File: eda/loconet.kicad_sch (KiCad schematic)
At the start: 78 parts, among them J1 RJ12, J10 DCC IN, J11 DCC1, J12 FROG3, J13 DCC4, J14 FROG4, J15 LN Debug, J16 LN Raw, J2 RJ12, J3 FROG1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

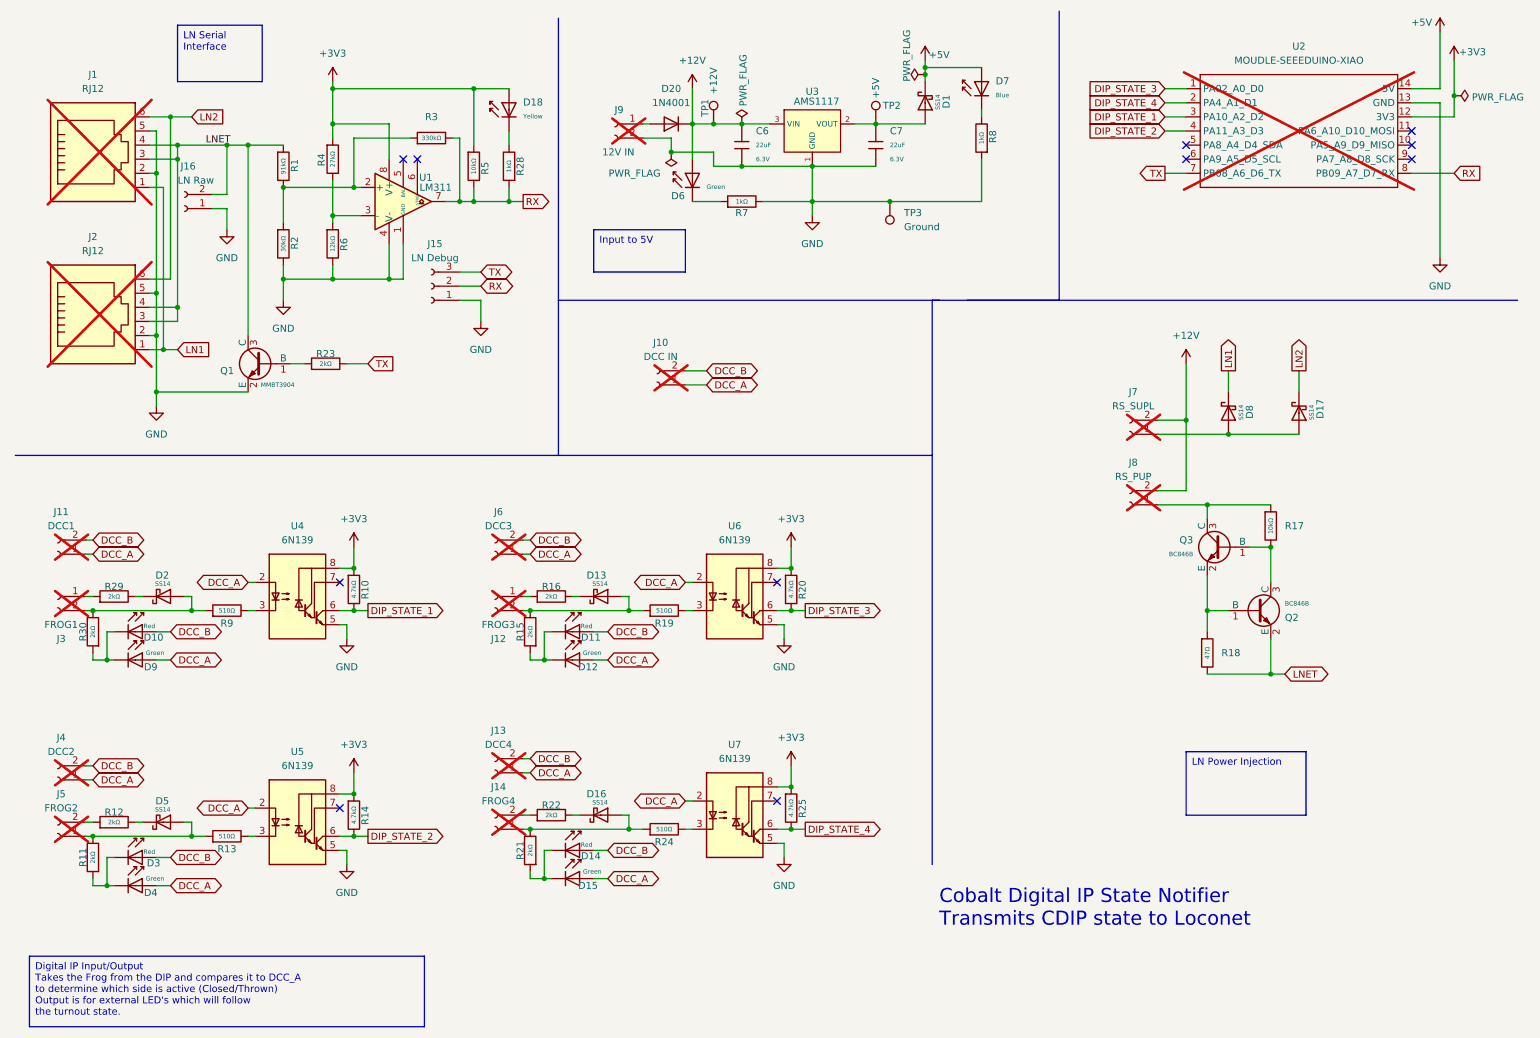
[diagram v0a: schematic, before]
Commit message: Fixups
* I removed the additional forwarding power part of the LN schematic. I don't think I was doing it right anyway. use a UP5 instead.
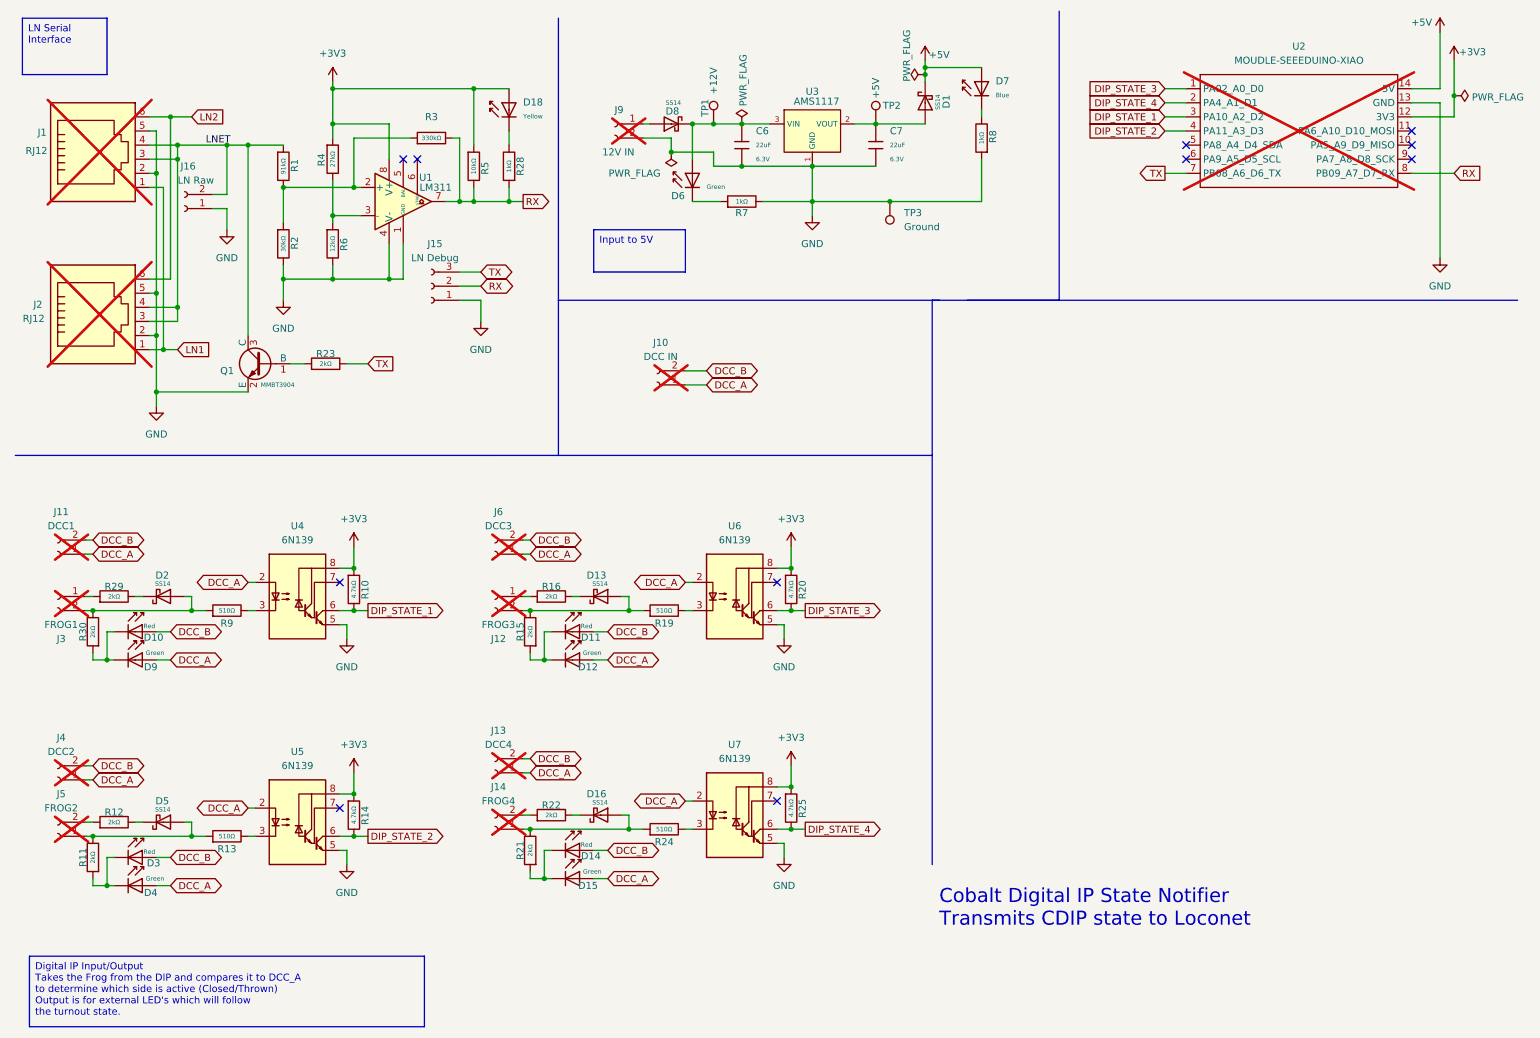
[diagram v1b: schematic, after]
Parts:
- removed D17: SS14, PCM_JLCPCB:D_SMA, symbol PCM_JLCPCB-Diodes:Schottky,SS14
- removed D20: 1N4001, Diode_THT:D_DO-41_SOD81_P10.16mm_Horizontal, symbol Diode:1N4001
- removed J7: RS_SUPL, Connector_PinHeader_2.54mm:PinHeader_1x02_P2.54mm_Vertical, symbol Connector:Conn_01x02_Socket
- removed J8: RS_PUP, Connector_PinHeader_2.54mm:PinHeader_1x02_P2.54mm_Vertical, symbol Connector:Conn_01x02_Socket
- removed Q2, Q3: BC846B, PCM_JLCPCB:Q_SOT-23, symbol PCM_JLCPCB-Transistors:NPN,BC846B
- removed R17: 10kΩ, PCM_JLCPCB:R_0603, symbol PCM_JLCPCB-Resistors:0603,10kΩ
- removed R18: 47Ω, PCM_JLCPCB:R_0603, symbol PCM_JLCPCB-Resistors:0603,47Ω
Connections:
- net LN1: no longer D8.1
- net at J9.1 (Pin_1): now also D8.2
- net +12V: no longer names the net of C6.1, D6.2, TP1.1, U3.3 (VIN)
- net +12V: now also D8.1

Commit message: Updating to the latest version of the board, still in KiCad 8.
* Bumped the README to be more readable.
* Removed second RJ12 jack, no more forwarding.
* Small changes to the ino.wq
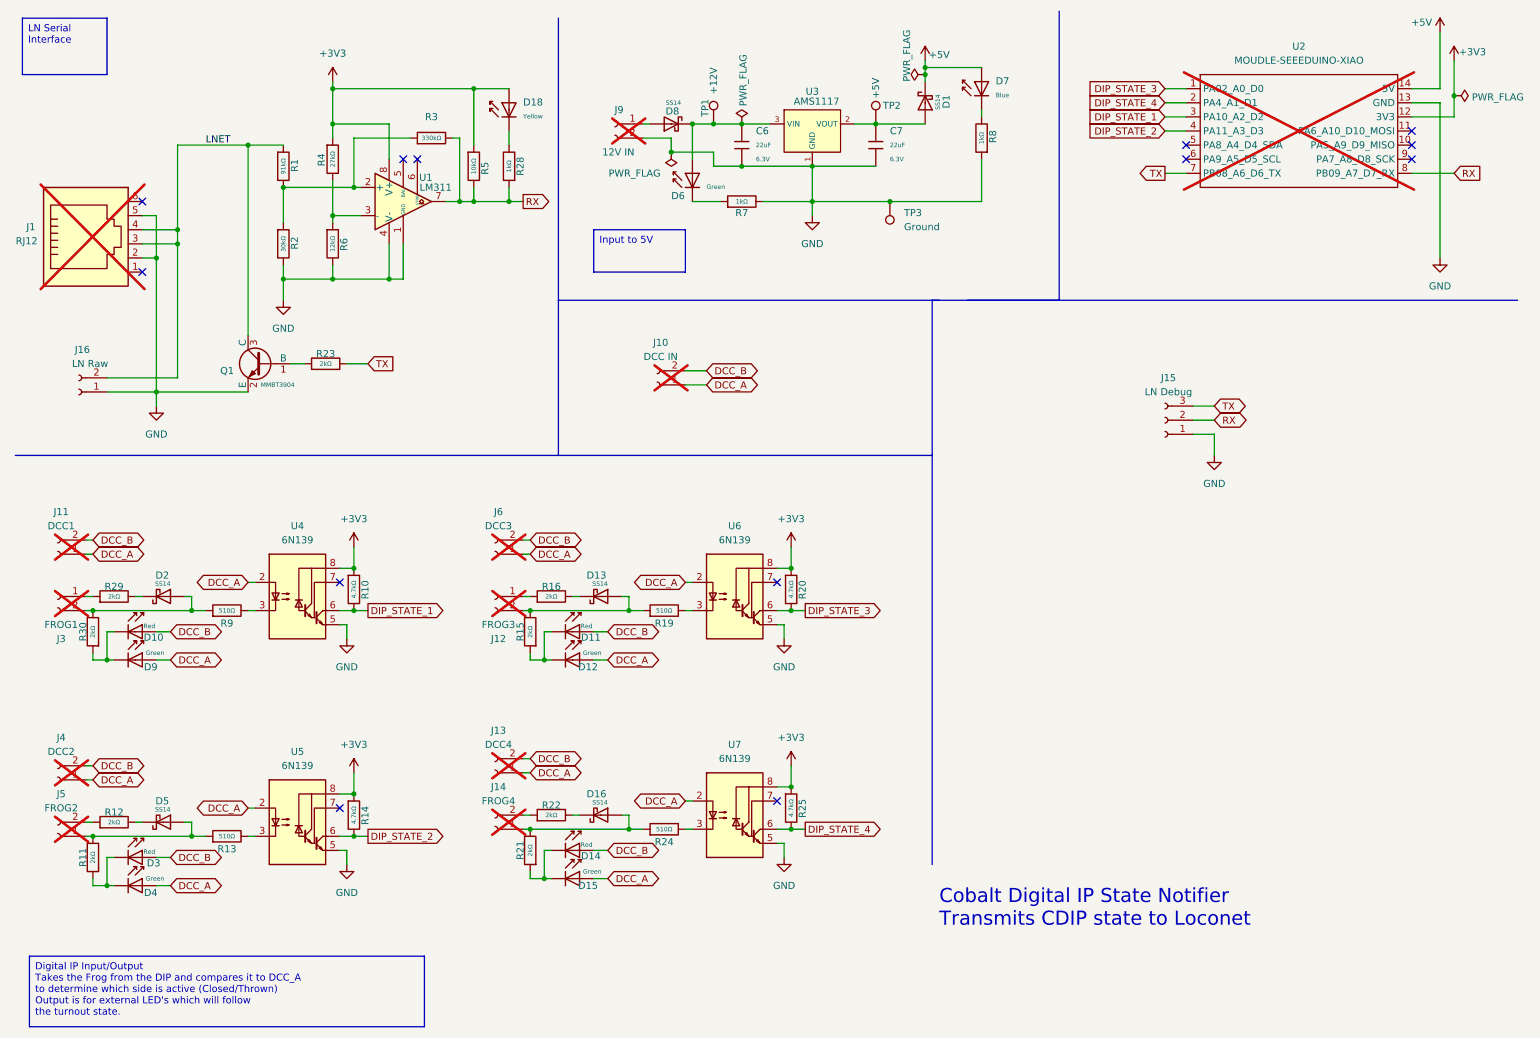
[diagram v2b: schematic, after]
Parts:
- removed J1: RJ12, Connector_RJ:RJ12_Amphenol_54601-x06_Horizontal, symbol Connector:RJ12
- renumbered J2 to J1
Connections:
- net LN1: no longer names the net of J1.1
- net LN2: no longer names the net of J1.6
- no-connect marks 11 -> 13
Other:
- moved on the sheet: J1, J15, J16

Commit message: Fixing issues with the layout after moving to KiCad 9
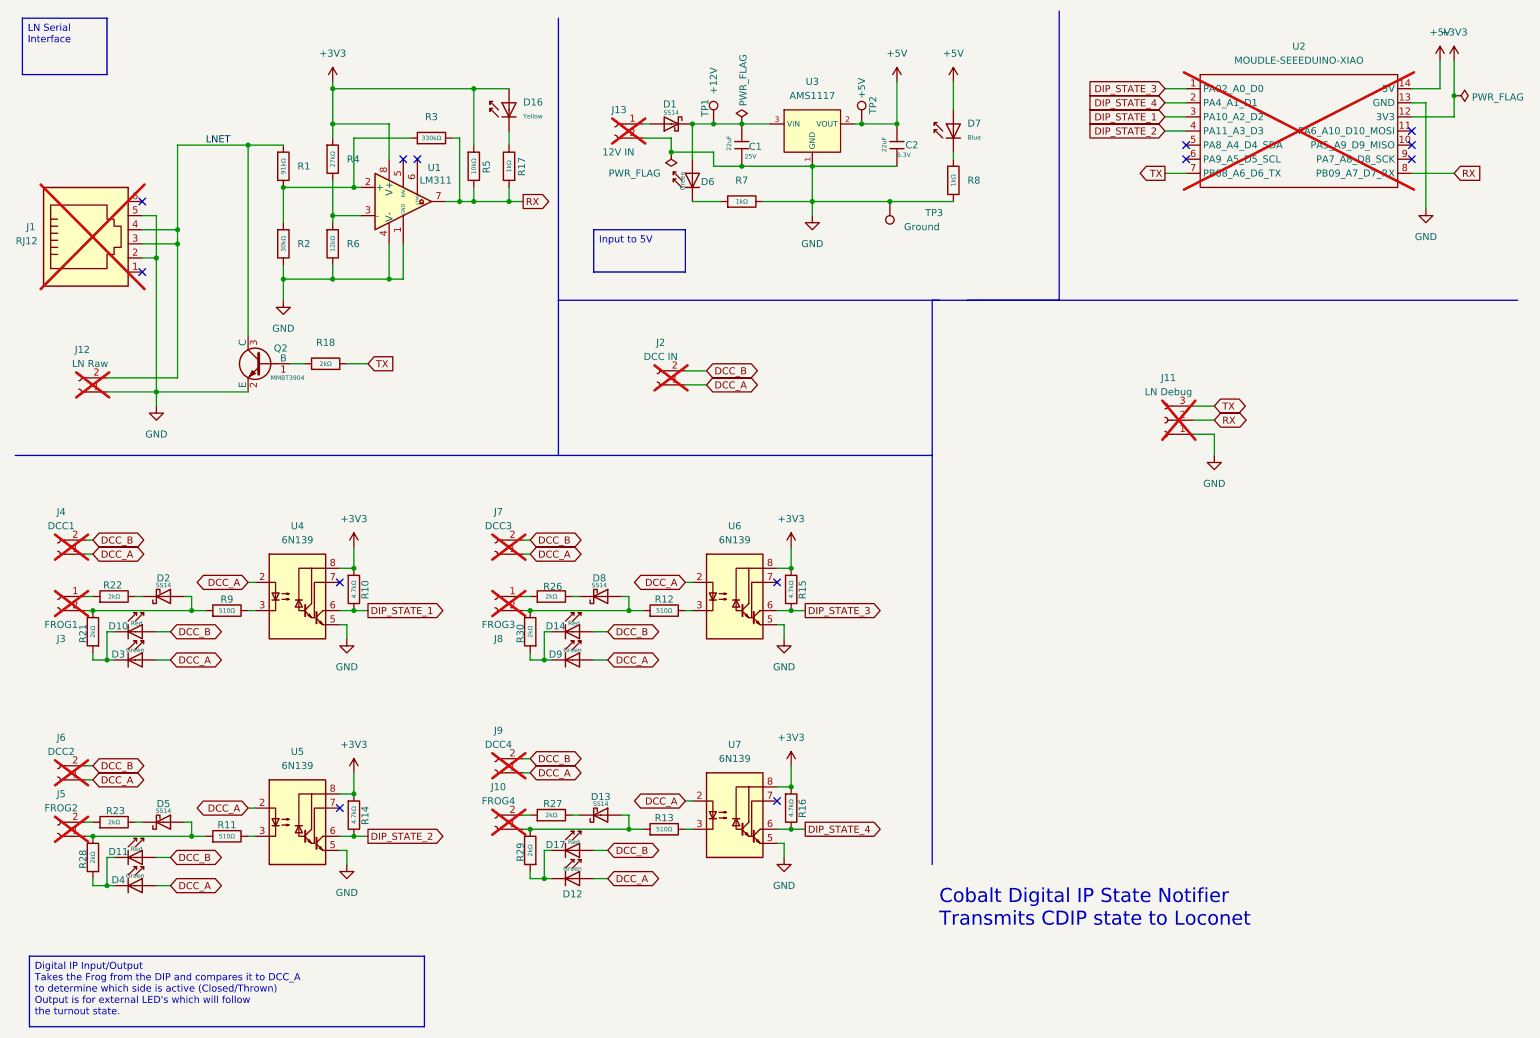
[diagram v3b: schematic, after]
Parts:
- removed C6, C7: 22uF, PCM_JLCPCB:C_0603, symbol PCM_JLCPCB-Capacitors:0603,22uF
- removed D15: Green, PCM_JLCPCB:D_0603, symbol PCM_JLCPCB-Diodes:LED,0603,Green
- removed D16: SS14, PCM_JLCPCB:D_SMA, symbol PCM_JLCPCB-Diodes:Schottky,SS14
- removed D18: Yellow, PCM_JLCPCB:D_0603, symbol PCM_JLCPCB-Diodes:LED,0603,Yellow
- removed D3: Red, PCM_JLCPCB:D_0603, symbol PCM_JLCPCB-Diodes:LED,0603,Red
- removed Q1: MMBT3904, PCM_JLCPCB:Q_SOT-23, symbol PCM_JLCPCB-Transistors:NPN,MMBT3904
- removed R11, R12, R15, R16: 2kΩ, PCM_JLCPCB:R_0402, symbol PCM_JLCPCB-Resistors:0402,2kΩ
- removed R13, R19, R24, R9: 510Ω, PCM_JLCPCB:R_0805, symbol PCM_JLCPCB-Resistors:0805,510Ω
- removed R20, R25: 4.7kΩ, PCM_JLCPCB:R_0402, symbol PCM_JLCPCB-Resistors:0402,4.7kΩ
- removed R28: 1kΩ, PCM_JLCPCB:R_0402, symbol PCM_JLCPCB-Resistors:0402,1kΩ
- removed R3: 330kΩ, PCM_JLCPCB:R_0402, symbol PCM_JLCPCB-Resistors:0402,330kΩ
- removed R5: 10kΩ, PCM_JLCPCB:R_0402, symbol PCM_JLCPCB-Resistors:0402,10kΩ
- added C1: 22uF, PCM_JLCPCB:C_0805, symbol PCM_JLCPCB-Capacitors:0805,22uF
- added C2: 22uF, PCM_JLCPCB:C_0603, symbol PCM_JLCPCB-Capacitors:0603,22uF
- added D16: Yellow, PCM_JLCPCB:D_0603, symbol PCM_JLCPCB-Diodes:LED,0603,Yellow
- added D17: Red, PCM_JLCPCB:D_0603, symbol PCM_JLCPCB-Diodes:LED,0603,Red
- added D3: Green, PCM_JLCPCB:D_0603, symbol PCM_JLCPCB-Diodes:LED,0603,Green
- added Q2: MMBT3904, PCM_JLCPCB:Q_SOT-23, symbol PCM_JLCPCB-Transistors:NPN,MMBT3904
- added R11, R12, R13, R9: 510Ω, PCM_JLCPCB:R_0603, symbol PCM_JLCPCB-Resistors:0603,510Ω
- added R15, R16: 4.7kΩ, PCM_JLCPCB:R_0402, symbol PCM_JLCPCB-Resistors:0402,4.7kΩ
- added R17: 1kΩ, PCM_JLCPCB:R_0402, symbol PCM_JLCPCB-Resistors:0402,1kΩ
- added R18, R26, R27, R28: 2kΩ, PCM_JLCPCB:R_0402, symbol PCM_JLCPCB-Resistors:0402,2kΩ
- added R3: 330kΩ, PCM_JLCPCB:R_0603, symbol PCM_JLCPCB-Resistors:0603,330kΩ
- added R5: 10kΩ, PCM_JLCPCB:R_0603, symbol PCM_JLCPCB-Resistors:0603,10kΩ
- D1, D13, D2, D5, D8: Stock 1067944 -> 1598447
- D10, D11, D14: Stock 2351029 -> 3650738
- D12, D4, D6, D9: Price 0.022USD -> 0.021USD; Stock 227581 -> 136525
- D7: Stock 226317 -> 9144
- J10: renamed from J14; footprint TerminalBlock_Phoenix:TerminalBlock_Phoenix_MKDS-1,5-2_1x02_P5.00mm_Horizontal -> TerminalBlock_Phoenix:TerminalBlock_Phoenix_MKDS-1,5-2-5.08_1x02_P5.08mm_Horizontal
- J11: renamed from J15; now not fitted; now left out of the parts list
- J12: renamed from J16; now not fitted; now left out of the parts list
- J13: renamed from J9; footprint TerminalBlock_Phoenix:TerminalBlock_Phoenix_MKDS-1,5-2_1x02_P5.00mm_Horizontal -> TerminalBlock_Phoenix:TerminalBlock_Phoenix_MKDS-1,5-2-5.08_1x02_P5.08mm_Horizontal
- J2: renamed from J10; footprint TerminalBlock_Phoenix:TerminalBlock_Phoenix_MKDS-1,5-2_1x02_P5.00mm_Horizontal -> TerminalBlock_Phoenix:TerminalBlock_Phoenix_MKDS-1,5-2-5.08_1x02_P5.08mm_Horizontal
- J3, J5: footprint TerminalBlock_Phoenix:TerminalBlock_Phoenix_MKDS-1,5-2_1x02_P5.00mm_Horizontal -> TerminalBlock_Phoenix:TerminalBlock_Phoenix_MKDS-1,5-2-5.08_1x02_P5.08mm_Horizontal
- J4: renamed from J11; footprint TerminalBlock_Phoenix:TerminalBlock_Phoenix_MKDS-1,5-2_1x02_P5.00mm_Horizontal -> TerminalBlock_Phoenix:TerminalBlock_Phoenix_MKDS-1,5-2-5.08_1x02_P5.08mm_Horizontal
- J6: renamed from J4; footprint TerminalBlock_Phoenix:TerminalBlock_Phoenix_MKDS-1,5-2_1x02_P5.00mm_Horizontal -> TerminalBlock_Phoenix:TerminalBlock_Phoenix_MKDS-1,5-2-5.08_1x02_P5.08mm_Horizontal
- J7: renamed from J6; footprint TerminalBlock_Phoenix:TerminalBlock_Phoenix_MKDS-1,5-2_1x02_P5.00mm_Horizontal -> TerminalBlock_Phoenix:TerminalBlock_Phoenix_MKDS-1,5-2-5.08_1x02_P5.08mm_Horizontal
- J8: renamed from J12; footprint TerminalBlock_Phoenix:TerminalBlock_Phoenix_MKDS-1,5-2_1x02_P5.00mm_Horizontal -> TerminalBlock_Phoenix:TerminalBlock_Phoenix_MKDS-1,5-2-5.08_1x02_P5.08mm_Horizontal
- J9: renamed from J13; footprint TerminalBlock_Phoenix:TerminalBlock_Phoenix_MKDS-1,5-2_1x02_P5.00mm_Horizontal -> TerminalBlock_Phoenix:TerminalBlock_Phoenix_MKDS-1,5-2-5.08_1x02_P5.08mm_Horizontal
- R1: Stock 318009 -> 221614
- R10, R14: Stock 5578116 -> 5094051
- R2: Stock 1632072 -> 952598
- R21, R22, R23, R29, R30: Stock 1795331 -> 1864367
- R4: Stock 736863 -> 414328
- R6: Stock 901273 -> 784104
- R7, R8: Stock 10799365 -> 5326005
- U3: Stock 35854 -> 72466
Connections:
- net +3V3: now also D16.2, R15.1, R16.1, R5.1
- net +5V: now also TP2.1, U3.2 (VOUT), C2.1; no longer D1.1
- net DCC_A: now also D3.2
- net DCC_B: now also D17.2
- net DIP_STATE_3: now also R15.2
- net DIP_STATE_4: now also R16.2
- net GND: now also R8.2, C1.2, C2.2, Q2.2 (E); no longer R8.1
- net LNET: now also Q2.3 (C)
- net RX: now also R17.1, R3.2, R5.2
- net TX: now also R18.2; no longer R23.2
- net at D5.2, J5.1 (Pin_1): now also R11.1, R28.2
- net at J5.2 (Pin_2): now also R23.1
- net at R21.2: now also D2.2, J3.2 (Pin_2), R9.1; no longer J10.1 (Pin_1)
- net at R22.1: now also J3.1 (Pin_1); no longer J10.2 (Pin_2)
- net at D11.1: now also D4.1, R28.1; no longer D12.1
- net at J8.2 (Pin_2): now also D8.2, R30.2, R12.1; no longer D13.2
- net at D14.1: now also D9.1, R30.1; no longer R21.1
- net at J13.1 (Pin_1): now also D1.2; no longer D8.2
- net at U5.3 (C2): now also R11.2
- net at R1.2, R2.1, U1.2 (+): now also R3.1
- net at R22.2: now also D2.1
- net at D6.2, TP1.1, U3.3 (VIN): now also D1.1, C1.1; no longer D8.1
- net at U4.3 (C2): now also R9.2
- net at U6.3 (C2): now also R12.2
- net at D5.1: now also R23.2
- net at J8.1 (Pin_1): now also R26.1
- net at R29.1: now also D12.1, D17.1; no longer J3.1 (Pin_1)
- net at D13.1: now also R27.2
- net at D7.1: now also R8.1; no longer R8.2
- net at R29.2: now also D13.2, J10.1 (Pin_1), R13.1; no longer D2.1
- net at U7.3 (C2): now also R13.2
- new net: D10.1, D3.1, R21.1
- new net: Q2.1 (B), R18.1
- new net: J10.2 (Pin_2), R27.1
- new net: D16.1, R17.2
- new net: D8.1, R26.2
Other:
- moved on the sheet: TP2
